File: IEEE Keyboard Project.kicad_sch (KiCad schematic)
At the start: 122 parts, among them U1 RP2354B

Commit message: Add files via upload
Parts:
- removed D1, D10, D11, D12, D13, D14, D15, D16, D17, D18, D19, D2, D20, D21, D22, D23, D24, D25, D26, D27, D28, D29, D3, D30, D31, D32, D33, D34, D35, D36, D37, D38, D39, D4, D40, D41, D42, D43, D44, D45, D46, D47, D48, D49, D5, D50, D51, D52, D53, D54, D55, D56, D6, D7, D8, D9: D_Small, symbol Device:D_Small
- removed MX1, MX10, MX11, MX12, MX13, MX14, MX15, MX16, MX17, MX18, MX19, MX2, MX20, MX21, MX22, MX23, MX24, MX25, MX26, MX27, MX28, MX29, MX3, MX30, MX31, MX32, MX33, MX34, MX35, MX36, MX37, MX38, MX39, MX4, MX40, MX41, MX42, MX43, MX44, MX45, MX46, MX47, MX48, MX49, MX5, MX50, MX51, MX52, MX53, MX54, MX55, MX56, MX6, MX7, MX8, MX9: MX_SW_HS, Button_Switch_Keyboard:SW_Cherry_MX_1.00u_PCB, symbol marbastlib-mx:MX_SW_HS_CPG151101S11
- added C10, C26, C27, C29: 4.7u, Capacitor_SMD:C_0402_1005Metric, symbol Device:C
- added C11, C22, C23, C24, C25, C28, C30, C31, C32, C33, C8: 100n, Capacitor_SMD:C_0402_1005Metric, symbol Device:C
- added C19, C21, C7, C9: 4.7u, RP2350_60QFN_minimal:C_0402_1005Metric_small_pads, symbol Device:C
- added C20, C3, C4, C5: 15p, Capacitor_SMD:C_0402_1005Metric, symbol Device:C
- added L1, L2: 3.3u, RP2350_60QFN_minimal:L_pol_2016, symbol Device:L
- added R10, R12, R6, R7, R8, R9: 1k, Resistor_SMD:R_0402_1005Metric, symbol Device:R
- added R11, R5: 33, Resistor_SMD:R_0402_1005Metric, symbol Device:R
- added R13, R14: 27, Resistor_SMD:R_0402_1005Metric, symbol Device:R
- added SW1, SW2, SW3, SW4: SW_Push, Button_Switch_SMD:SW_Push_1P1T_NO_Vertical_Wuerth_434133025816, symbol Switch:SW_Push
- added U2: RP2354B, Package_DFN_QFN:QFN-80-1EP_10x10mm_P0.4mm_EP3.4x3.4mm, symbol MCU_RaspberryPi:RP2354B
- added Y1, Y2: ABM8-272-T3, Crystal:Crystal_SMD_3225-4Pin_3.2x2.5mm, symbol Device:Crystal_GND24
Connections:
- net +3V3: now also U1.64 (VREG_VIN), C19.1, C22.1, C23.1, C24.1, C28.1, C30.1, C32.1, C33.1, C7.1, R11.1, R5.1, U2.64 (VREG_VIN)
- net COL0: now also U1.79 (GPIO2)
- net COL1: now also U1.80 (GPIO3)
- net COL10: now also U2.2 (GPIO5)
- net COL11: now also U2.3 (GPIO6)
- net COL12: now also U2.4 (GPIO7)
- net COL13: now also U2.6 (GPIO8)
- net COL2: now also U1.1 (GPIO4)
- net COL3: now also U1.2 (GPIO5)
- net COL4: now also U1.3 (GPIO6)
- net COL5: now also U1.4 (GPIO7)
- net COL6: now also U1.6 (GPIO8)
- net COL7: now also U2.79 (GPIO2)
- net COL8: now also U2.80 (GPIO3)
- net COL9: now also U2.1 (GPIO4)
- net GND: now also U1.15 (IOVDD), U1.24 (IOVDD), U1.29 (IOVDD), U1.41 (IOVDD), U1.5 (IOVDD), U1.50 (IOVDD), U1.59 (ADC_AVDD), U1.60 (IOVDD), U1.62 (VREG_PGND), U1.68 (USB_OTP_VDD), U1.69 (QSPI_IOVDD), U1.76 (IOVDD), U1.81 (GND), C10.2, C11.2, C19.2, C20.2, C21.2, C22.2, C23.2, C24.2, C25.2, C26.2, C27.2, C28.2, C29.2, C3.2, C30.2, C31.2, C32.2, C33.2, C4.2, C5.2, C7.2, C8.2, C9.2, R8.2, R9.2, SW1.1, SW3.1, U2.15 (IOVDD), U2.24 (IOVDD), U2.29 (IOVDD), U2.41 (IOVDD), U2.5 (IOVDD), U2.50 (IOVDD), U2.59 (ADC_AVDD), U2.60 (IOVDD), U2.62 (VREG_PGND), U2.68 (USB_OTP_VDD), U2.69 (QSPI_IOVDD), U2.76 (IOVDD), U2.81 (GND), Y1.2, Y1.4, Y2.2, Y2.4
- net ROW0: now also U1.7 (GPIO9)
- net ROW1: now also U1.8 (GPIO10)
- net ROW2: now also U1.9 (GPIO11)
- net ROW3: now also U1.11 (GPIO12)
- net ROW4: now also U1.12 (GPIO13)
- net ROW5: now also U2.7 (GPIO9)
- net ROW6: now also U2.8 (GPIO10)
- net ROW7: now also U2.9 (GPIO11)
- net ROW8: now also U2.11 (GPIO12)
- net ROW9: now also U2.12 (GPIO13)
- net USB_D+: now also R13.2
- net USB_D-: now also R14.2
- net at U1.10 (DVDD), U1.32 (DVDD), U1.51 (DVDD): now also C10.1, C11.1, C8.1
- net XIN: now reaches U1.30 (XIN)
- net XIN: now also C3.1, C5.1, U2.30 (XIN), Y1.1, Y2.1
- net XOUT: now reaches U1.31 (XOUT)
- net XOUT: now also R12.1, R7.1, U2.31 (XOUT)
- net at U1.35 (RUN): now also SW2.2
- net VREG_AVDD: now reaches U1.61 (VREG_AVDD)
- net VREG_AVDD: now also C26.1, C27.1, R11.2, R5.2, U2.61 (VREG_AVDD)
- net VREG_LX: now reaches U1.63 (VREG_LX)
- net VREG_LX: now also L1.2
- net +1V1: now reaches U1.65 (VREG_FB)
- net +1V1: now also C21.1, C9.1, L1.1, L2.1, U2.65 (VREG_FB)
- net at U1.75 (~{QSPI_SS}): now also R6.1
- net UART0 TX: now reaches U1.77 (GPIO0)
- net UART0 TX: now also U2.77 (GPIO0)
- net UART0 RX: now reaches U1.78 (GPIO1)
- net UART0 RX: now also U2.78 (GPIO1)
- new net: C25.1, C29.1, C31.1, U2.10 (DVDD), U2.32 (DVDD), U2.51 (DVDD)
- new net: R9.1, SW4.1
- new net: SW4.2, U2.35 (RUN)
- new net: R10.1, U2.75 (~{QSPI_SS})
- new net: R10.2, SW3.2
- new net: R8.1, SW2.1
- new net: C20.1, R12.2, Y2.3
- new net: R6.2, SW1.2
- new net: C4.1, R7.2, Y1.3
- new net: R13.1, U2.66 (USB_DM)
- new net: R14.1, U2.67 (USB_DP)
- new net VREG_LX2: L2.2, U2.63 (VREG_LX)
- no-connect marks 0 -> 82
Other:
- added sheet Keyboard Matrix (Keyboard_Matrix.kicad_sch)
- note added: "12MHz Crystal"
- moved on the sheet: C12, C13, C14, C15, C16, C17, C18, R1, R2, U1

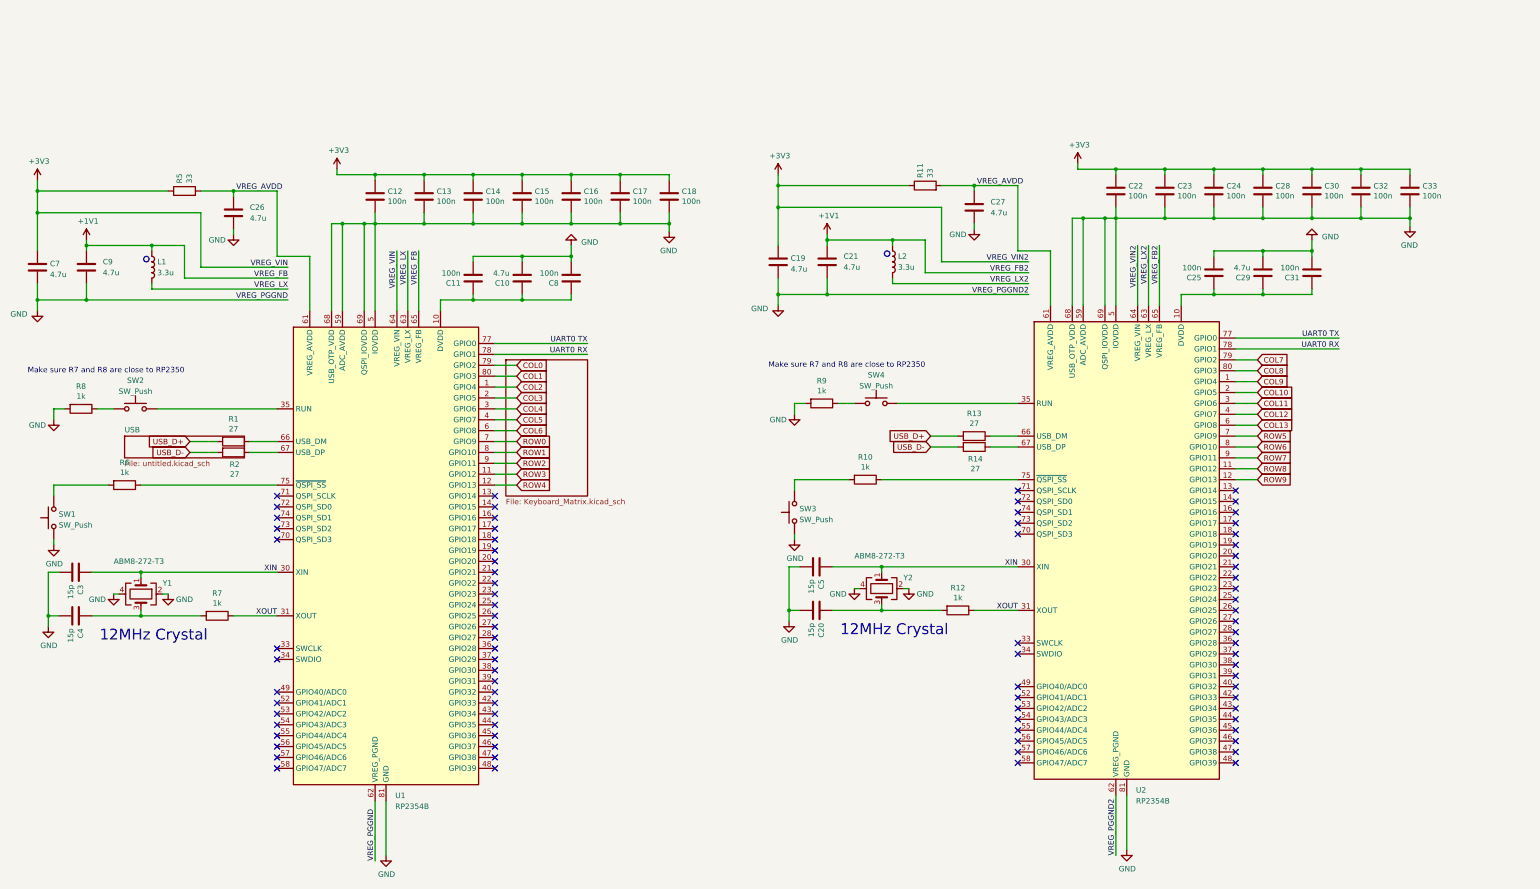
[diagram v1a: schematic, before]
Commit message: Finalized schematic and most updated PCB Layout
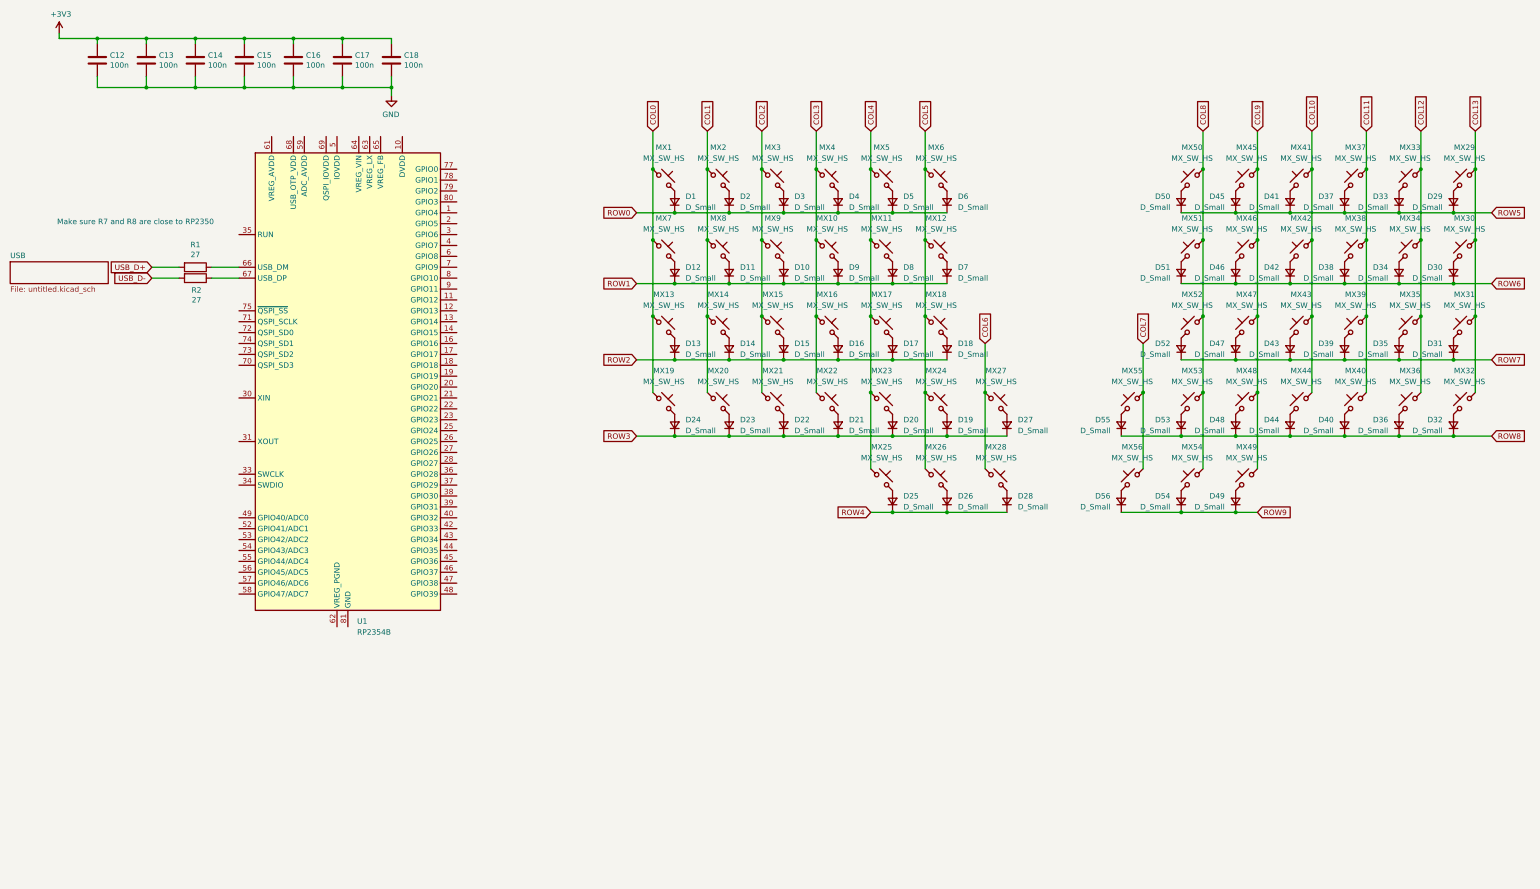
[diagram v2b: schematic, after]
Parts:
- removed C10, C26, C27, C29: 4.7u, Capacitor_SMD:C_0402_1005Metric, symbol Device:C
- removed C11, C22, C23, C24, C25, C28, C30, C31, C32, C33, C8: 100n, Capacitor_SMD:C_0402_1005Metric, symbol Device:C
- removed C19, C21, C7, C9: 4.7u, RP2350_60QFN_minimal:C_0402_1005Metric_small_pads, symbol Device:C
- removed C20, C3, C4, C5: 15p, Capacitor_SMD:C_0402_1005Metric, symbol Device:C
- removed L1, L2: 3.3u, RP2350_60QFN_minimal:L_pol_2016, symbol Device:L
- removed R10, R12, R6, R7, R8, R9: 1k, Resistor_SMD:R_0402_1005Metric, symbol Device:R
- removed R11, R5: 33, Resistor_SMD:R_0402_1005Metric, symbol Device:R
- removed R13, R14: 27, Resistor_SMD:R_0402_1005Metric, symbol Device:R
- removed SW1, SW2, SW3, SW4: SW_Push, Button_Switch_SMD:SW_Push_1P1T_NO_Vertical_Wuerth_434133025816, symbol Switch:SW_Push
- removed U2: RP2354B, Package_DFN_QFN:QFN-80-1EP_10x10mm_P0.4mm_EP3.4x3.4mm, symbol MCU_RaspberryPi:RP2354B
- removed Y1, Y2: ABM8-272-T3, Crystal:Crystal_SMD_3225-4Pin_3.2x2.5mm, symbol Device:Crystal_GND24
- added D1, D10, D11, D12, D13, D14, D15, D16, D17, D18, D19, D2, D20, D21, D22, D23, D24, D25, D26, D27, D28, D29, D3, D30, D31, D32, D33, D34, D35, D36, D37, D38, D39, D4, D40, D41, D42, D43, D44, D45, D46, D47, D48, D49, D5, D50, D51, D52, D53, D54, D55, D56, D6, D7, D8, D9: D_Small, symbol Device:D_Small
- added MX1, MX10, MX11, MX12, MX13, MX14, MX15, MX16, MX17, MX18, MX19, MX2, MX20, MX21, MX22, MX23, MX24, MX25, MX26, MX27, MX28, MX29, MX3, MX30, MX31, MX32, MX33, MX34, MX35, MX36, MX37, MX38, MX39, MX4, MX40, MX41, MX42, MX43, MX44, MX45, MX46, MX47, MX48, MX49, MX5, MX50, MX51, MX52, MX53, MX54, MX55, MX56, MX6, MX7, MX8, MX9: MX_SW_HS, Button_Switch_Keyboard:SW_Cherry_MX_1.00u_PCB, symbol marbastlib-mx:MX_SW_HS_CPG151101S11
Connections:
- net +3V3: no longer U1.64 (VREG_VIN)
- net COL0: now also MX1.1, MX13.1, MX19.1, MX7.1; no longer U1.79 (GPIO2)
- net COL1: now also MX14.1, MX2.1, MX20.1, MX8.1; no longer U1.80 (GPIO3)
- net COL10: now also MX41.1, MX42.1, MX43.1, MX44.1
- net COL11: now also MX37.1, MX38.1, MX39.1, MX40.1
- net COL12: now also MX33.1, MX34.1, MX35.1, MX36.1
- net COL13: now also MX29.1, MX30.1, MX31.1, MX32.1
- net COL2: now also MX15.1, MX21.1, MX3.1, MX9.1; no longer U1.1 (GPIO4)
- net COL3: now also MX10.1, MX16.1, MX22.1, MX4.1; no longer U1.2 (GPIO5)
- net COL4: now also MX11.1, MX17.1, MX23.1, MX25.1, MX5.1; no longer U1.3 (GPIO6)
- net COL5: now also MX12.1, MX18.1, MX24.1, MX26.1, MX6.1; no longer U1.4 (GPIO7)
- net COL6: now also MX27.1, MX28.1; no longer U1.6 (GPIO8)
- net COL7: now also MX55.1, MX56.1
- net COL8: now also MX50.1, MX51.1, MX52.1, MX53.1, MX54.1
- net COL9: now also MX45.1, MX46.1, MX47.1, MX48.1, MX49.1
- net GND: no longer U1.15 (IOVDD), U1.24 (IOVDD), U1.29 (IOVDD), U1.41 (IOVDD), U1.5 (IOVDD), U1.50 (IOVDD), U1.59 (ADC_AVDD), U1.60 (IOVDD), U1.62 (VREG_PGND), U1.68 (USB_OTP_VDD), U1.69 (QSPI_IOVDD), U1.76 (IOVDD), U1.81 (GND)
- net ROW0: now also D1.1 (K), D2.1 (K), D3.1 (K), D4.1 (K), D5.1 (K), D6.1 (K); no longer U1.7 (GPIO9)
- net ROW1: now also D10.1 (K), D11.1 (K), D12.1 (K), D7.1 (K), D8.1 (K), D9.1 (K); no longer U1.8 (GPIO10)
- net ROW2: now also D13.1 (K), D14.1 (K), D15.1 (K), D16.1 (K), D17.1 (K), D18.1 (K); no longer U1.9 (GPIO11)
- net ROW3: now also D19.1 (K), D20.1 (K), D21.1 (K), D22.1 (K), D23.1 (K), D24.1 (K), D27.1 (K); no longer U1.11 (GPIO12)
- net ROW4: now also D25.1 (K), D26.1 (K), D28.1 (K); no longer U1.12 (GPIO13)
- net ROW5: now also D29.1 (K), D33.1 (K), D37.1 (K), D41.1 (K), D45.1 (K), D50.1 (K)
- net ROW6: now also D30.1 (K), D34.1 (K), D38.1 (K), D42.1 (K), D46.1 (K), D51.1 (K)
- net ROW7: now also D31.1 (K), D35.1 (K), D39.1 (K), D43.1 (K), D47.1 (K), D52.1 (K)
- net ROW8: now also D32.1 (K), D36.1 (K), D40.1 (K), D44.1 (K), D48.1 (K), D53.1 (K), D55.1 (K)
- net ROW9: now also D49.1 (K), D54.1 (K), D56.1 (K)
- net +1V1: no longer names the net of U1.65 (VREG_FB)
- net UART0 RX: no longer names the net of U1.78 (GPIO1)
- net UART0 TX: no longer names the net of U1.77 (GPIO0)
- net VREG_AVDD: no longer names the net of U1.61 (VREG_AVDD)
- net VREG_LX: no longer names the net of U1.63 (VREG_LX)
- net XIN: no longer names the net of U1.30 (XIN)
- net XOUT: no longer names the net of U1.31 (XOUT)
- new net: D23.2 (A), MX20.2
- new net: D42.2 (A), MX42.2
- new net: D34.2 (A), MX34.2
- new net: D53.2 (A), MX53.2
- new net: D22.2 (A), MX21.2
- new net: D3.2 (A), MX3.2
- new net: D36.2 (A), MX36.2
- new net: D47.2 (A), MX47.2
- new net: D27.2 (A), MX27.2
- new net: D25.2 (A), MX25.2
- new net: D15.2 (A), MX15.2
- new net: D49.2 (A), MX49.2
- new net: D52.2 (A), MX52.2
- new net: D31.2 (A), MX31.2
- new net: D7.2 (A), MX12.2
- new net: D55.2 (A), MX55.2
- new net: D45.2 (A), MX45.2
- new net: D33.2 (A), MX33.2
- new net: D6.2 (A), MX6.2
- new net: D28.2 (A), MX28.2
- new net: D8.2 (A), MX11.2
- new net: D2.2 (A), MX2.2
- new net: D37.2 (A), MX37.2
- new net: D20.2 (A), MX23.2
- new net: D48.2 (A), MX48.2
- new net: D5.2 (A), MX5.2
- new net: D24.2 (A), MX19.2
- new net: D14.2 (A), MX14.2
- new net: U1.15 (IOVDD), U1.24 (IOVDD), U1.29 (IOVDD), U1.41 (IOVDD), U1.5 (IOVDD), U1.50 (IOVDD), U1.60 (IOVDD), U1.76 (IOVDD)
- new net: D26.2 (A), MX26.2
- new net: D32.2 (A), MX32.2
- new net: D12.2 (A), MX7.2
- new net: D41.2 (A), MX41.2
- new net: D39.2 (A), MX39.2
- new net: D19.2 (A), MX24.2
- new net: D35.2 (A), MX35.2
- new net: D11.2 (A), MX8.2
- new net: D10.2 (A), MX9.2
- new net: D1.2 (A), MX1.2
- new net: D56.2 (A), MX56.2
- new net: D30.2 (A), MX30.2
- new net: D9.2 (A), MX10.2
- new net: D54.2 (A), MX54.2
- new net: D50.2 (A), MX50.2
- new net: D29.2 (A), MX29.2
- new net: D46.2 (A), MX46.2
- new net: D21.2 (A), MX22.2
- new net: D43.2 (A), MX43.2
- new net: D18.2 (A), MX18.2
- new net: D40.2 (A), MX40.2
- new net: D4.2 (A), MX4.2
- new net: D38.2 (A), MX38.2
- new net: D17.2 (A), MX17.2
- new net: D16.2 (A), MX16.2
- new net: D44.2 (A), MX44.2
- new net: D51.2 (A), MX51.2
- new net: D13.2 (A), MX13.2
- no-connect marks 82 -> 0
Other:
- removed sheet Keyboard Matrix
- note removed: "12MHz Crystal"
- moved on the sheet: C12, C13, C14, C15, C16, C17, C18, R1, R2, U1
